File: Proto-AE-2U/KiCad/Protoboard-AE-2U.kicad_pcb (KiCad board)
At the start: 2 copper layers, 1 part

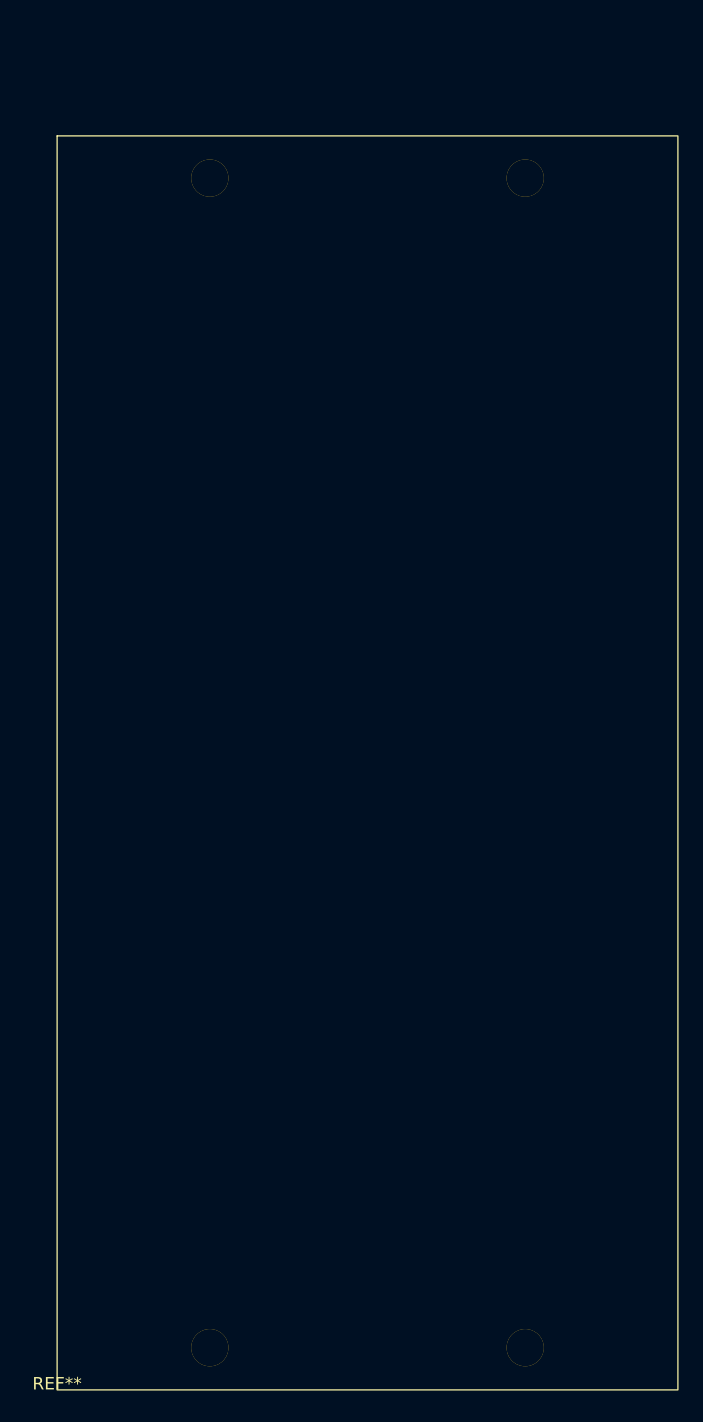
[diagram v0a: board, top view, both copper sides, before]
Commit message: copied 1U protoboard 2U and will adapt
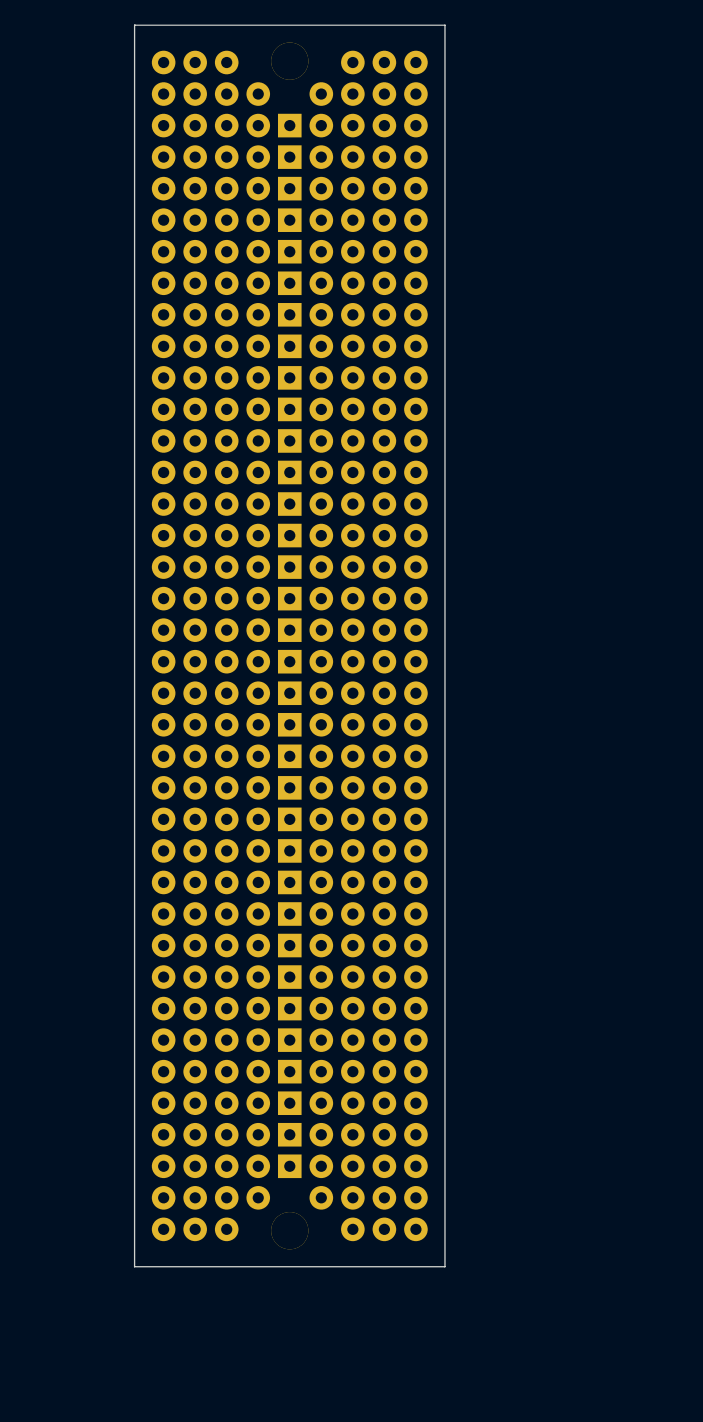
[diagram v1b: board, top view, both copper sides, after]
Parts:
- removed the REF** at (76.5, 144.0)
- added REF**: Pad, clectric-diy:Pad, F.Cu at (100.3, 47.2)
- added REF**: Pad, clectric-diy:Pad, F.Cu at (102.9, 42.2)
- added REF**: Pad, clectric-diy:Pad, F.Cu at (95.2, 95.5)
- added REF**: Pad, clectric-diy:Pad, F.Cu at (85.1, 42.2)
- added REF**: Pad, clectric-diy:Pad, F.Cu at (105.4, 54.9)
- added REF**: Pad, clectric-diy:Pad, F.Cu at (95.2, 85.3)
- added REF**: Pad, clectric-diy:Pad, F.Cu at (102.9, 44.7)
- added REF**: Pad, clectric-diy:Pad, F.Cu at (100.3, 108.2)
- added REF**: Pad, clectric-diy:Pad, F.Cu at (87.6, 100.6)
- added REF**: Pad, clectric-diy:Pad, F.Cu at (95.2, 67.6)
- added REF**: Pad, clectric-diy:Pad, F.Cu at (102.9, 80.3)
- added REF**: Pad, clectric-diy:Pad, F.Cu at (102.9, 57.4)
- added REF**: Pad, clectric-diy:Pad, F.Cu at (100.3, 103.1)
- added REF**: Pad, clectric-diy:Pad, F.Cu at (87.6, 115.8)
- added REF**: Pad, clectric-diy:Pad, F.Cu at (105.4, 110.8)
- added REF**: Pad, clectric-diy:Pad, F.Cu at (92.7, 75.2)
- added REF**: Pad, clectric-diy:Pad, F.Cu at (87.6, 49.8)
- added REF**: Pad, clectric-diy:Pad, F.Cu at (90.2, 57.4)
- added REF**: Pad, clectric-diy:Pad, F.Cu at (95.2, 103.1)
- added REF**: Pad, clectric-diy:Pad, F.Cu at (87.6, 44.7)
- added REF**: Pad, clectric-diy:Pad, F.Cu at (85.1, 82.8)
- added REF**: Pad, clectric-diy:Pad, F.Cu at (97.8, 42.2)
- added REF**: Pad, clectric-diy:Pad, F.Cu at (95.2, 123.5)
- added REF**: Pad, clectric-diy:Pad, F.Cu at (85.1, 47.2)
- added REF**: Pad, clectric-diy:Pad, F.Cu at (100.3, 93.0)
- added REF**: Pad, clectric-diy:Pad, F.Cu at (92.7, 110.8)
- added REF**: Pad, clectric-diy:Pad, F.Cu at (97.8, 85.3)
- added REF**: Pad, clectric-diy:Pad, F.Cu at (102.9, 113.3)
- added REF**: Pad, clectric-diy:Pad, F.Cu at (85.1, 37.1)
- added REF**: Pad, clectric-diy:Pad, F.Cu at (105.4, 123.5)
- added REF**: Pad, clectric-diy:Pad, F.Cu at (95.2, 113.3)
- added REF**: Pad, clectric-diy:Pad, F.Cu at (85.1, 80.3)
- added REF**: Pad, clectric-diy:Pad, F.Cu at (97.8, 115.8)
- added REF**: Pad, clectric-diy:Pad, F.Cu at (95.2, 47.2)
- added REF**: Pad, clectric-diy:Pad, F.Cu at (85.1, 98.0)
- added REF**: Pad, clectric-diy:Pad, F.Cu at (92.7, 105.7)
- added REF**: Pad, clectric-diy:Pad, F.Cu at (85.1, 49.8)
- added REF**: Pad, clectric-diy:Pad, F.Cu at (102.9, 75.2)
- added REF**: Pad, clectric-diy:Pad, F.Cu at (87.6, 39.6)
- added REF**: Pad, clectric-diy:Pad, F.Cu at (92.7, 100.6)
- added REF**: Pad, clectric-diy:Pad, F.Cu at (100.3, 87.9)
- added REF**: Pad, clectric-diy:Pad, F.Cu at (105.4, 47.2)
- added REF**: Pad, clectric-diy:Pad, F.Cu at (90.2, 85.3)
- added REF**: Pad, clectric-diy:Pad, F.Cu at (90.2, 105.7)
- added REF**: Pad, clectric-diy:Pad, F.Cu at (100.3, 67.6)
- added REF**: Pad, clectric-diy:Pad, F.Cu at (87.6, 85.3)
- added REF**: Pad, clectric-diy:Pad, F.Cu at (97.8, 52.3)
- added REF**: Pad, clectric-diy:Pad, F.Cu at (100.3, 90.4)
- added REF**: Pad, clectric-diy:Pad, F.Cu at (95.2, 118.4)
- added REF**: Pad, clectric-diy:Pad, F.Cu at (90.2, 113.3)
- added REF**: Pad, clectric-diy:Pad, F.Cu at (87.6, 98.0)
- added REF**: Pad, clectric-diy:Pad, F.Cu at (95.2, 49.8)
- added REF**: Pad, clectric-diy:Pad, F.Cu at (105.4, 113.3)
- added REF**: Pad, clectric-diy:Pad, F.Cu at (100.3, 72.7)
- added REF**: Pad, clectric-diy:Pad, F.Cu at (97.8, 80.3)
- added REF**: Pad, clectric-diy:Pad, F.Cu at (90.2, 118.4)
- added REF**: Pad, clectric-diy:Pad, F.Cu at (105.4, 95.5)
- added REF**: Pad, clectric-diy:Pad, F.Cu at (87.6, 70.1)
- added REF**: Pad, clectric-diy:Pad, F.Cu at (87.6, 128.5)
- added REF**: Pad, clectric-diy:Pad, F.Cu at (100.3, 98.0)
- added REF**: Pad, clectric-diy:Pad, F.Cu at (87.6, 60.0)
- added REF**: Pad, clectric-diy:Pad, F.Cu at (97.8, 57.4)
- added REF**: Pad, clectric-diy:Pad, F.Cu at (97.8, 100.6)
- added REF**: Pad, clectric-diy:Pad, F.Cu at (105.4, 77.7)
- added REF**: Pad, clectric-diy:Pad, F.Cu at (90.2, 90.4)
- added REF**: Pad, clectric-diy:Pad, F.Cu at (87.6, 131.1)
- added REF**: Pad, clectric-diy:Pad, F.Cu at (105.4, 98.0)
- added REF**: Pad, clectric-diy:Pad, F.Cu at (85.1, 128.5)
- added REF**: Pad, clectric-diy:Pad, F.Cu at (90.2, 47.2)
- added REF**: Pad, clectric-diy:Pad, F.Cu at (95.2, 52.3)
- added REF**: Pad, clectric-diy:Pad, F.Cu at (87.6, 37.1)
- added REF**: Pad, clectric-diy:Pad, F.Cu at (92.7, 95.5)
- added REF**: Pad, clectric-diy:Pad, F.Cu at (95.2, 136.2)
- added REF**: Pad, clectric-diy:Pad, F.Cu at (97.8, 39.6)
- added REF**: Pad, clectric-diy:Pad, F.Cu at (92.7, 85.3)
- added REF**: Pad, clectric-diy:Pad, F.Cu at (97.8, 67.6)
- added REF**: Pad, clectric-diy:Pad, F.Cu at (92.7, 93.0)
- added REF**: Pad, clectric-diy:Pad, F.Cu at (95.2, 60.0)
- added REF**: Pad, clectric-diy:Pad, F.Cu at (87.6, 123.5)
- added REF**: Pad, clectric-diy:Pad, F.Cu at (85.1, 87.9)
- added REF**: Pad, clectric-diy:Pad, F.Cu at (105.4, 128.5)
- added REF**: Pad, clectric-diy:Pad, F.Cu at (100.3, 110.8)
- added REF**: Pad, clectric-diy:Pad, F.Cu at (100.3, 42.2)
- added REF**: Pad, clectric-diy:Pad, F.Cu at (102.9, 70.1)
- added REF**: Pad, clectric-diy:Pad, F.Cu at (105.4, 57.4)
- added REF**: Pad, clectric-diy:Pad, F.Cu at (90.2, 120.9)
- added REF**: Pad, clectric-diy:Pad, F.Cu at (102.9, 52.3)
- added REF**: Pad, clectric-diy:Pad, F.Cu at (95.2, 62.5)
- added REF**: Pad, clectric-diy:Pad, F.Cu at (85.1, 85.3)
- added REF**: Pad, clectric-diy:Pad, F.Cu at (87.6, 126.0)
- added REF**: Pad, clectric-diy:Pad, F.Cu at (90.2, 100.6)
- added REF**: Pad, clectric-diy:Pad, F.Cu at (90.2, 93.0)
- added REF**: Pad, clectric-diy:Pad, F.Cu at (95.2, 108.2)
- added REF**: Pad, clectric-diy:Pad, F.Cu at (100.3, 54.9)
- added REF**: Pad, clectric-diy:Pad, F.Cu at (90.2, 115.8)
- added REF**: Pad, clectric-diy:Pad, F.Cu at (102.9, 90.4)
- added REF**: Pad, clectric-diy:Pad, F.Cu at (95.2, 105.7)
- added REF**: Pad, clectric-diy:Pad, F.Cu at (100.3, 60.0)
- added REF**: Pad, clectric-diy:Pad, F.Cu at (97.8, 93.0)
- added REF**: Pad, clectric-diy:Pad, F.Cu at (90.2, 110.8)
- added REF**: Pad, clectric-diy:Pad, F.Cu at (100.3, 39.6)
- added REF**: Pad, clectric-diy:Pad, F.Cu at (90.2, 62.5)
- added REF**: Pad, clectric-diy:Pad, F.Cu at (105.4, 85.3)
- added REF**: Pad, clectric-diy:Pad, F.Cu at (102.9, 72.7)
- added REF**: Pad, clectric-diy:Pad, F.Cu at (87.6, 118.4)
- added REF**: Pad, clectric-diy:Pad, F.Cu at (92.7, 118.4)
- added REF**: Pad, clectric-diy:Pad, F.Cu at (105.4, 126.0)
- added REF**: Pad, clectric-diy:Pad, F.Cu at (100.3, 49.8)
- added REF**: Pad, clectric-diy:Pad, F.Cu at (92.7, 72.7)
- added REF**: Pad, clectric-diy:Pad, F.Cu at (90.2, 42.2)
- added REF**: Pad, clectric-diy:Pad, F.Cu at (105.4, 103.1)
- added REF**: Pad, clectric-diy:Pad, F.Cu at (90.2, 60.0)
- added REF**: Pad, clectric-diy:Pad, F.Cu at (100.3, 80.3)
- added REF**: Pad, clectric-diy:Pad, F.Cu at (97.8, 105.7)
- added REF**: Pad, clectric-diy:Pad, F.Cu at (100.3, 62.5)
- added REF**: Pad, clectric-diy:Pad, F.Cu at (90.2, 72.7)
- added REF**: Pad, clectric-diy:Pad, F.Cu at (105.4, 118.4)
- added REF**: Pad, clectric-diy:Pad, F.Cu at (85.1, 39.6)
- added REF**: Pad, clectric-diy:Pad, F.Cu at (95.2, 77.7)
- added REF**: Pad, clectric-diy:Pad, F.Cu at (90.2, 49.8)
- added REF**: Pad, clectric-diy:Pad, F.Cu at (105.4, 115.8)
- added REF**: Pad, clectric-diy:Pad, F.Cu at (95.2, 98.0)
- added REF**: Pad, clectric-diy:Pad, F.Cu at (97.8, 113.3)
- added REF**: Pad, clectric-diy:Pad, F.Cu at (97.8, 110.8)
- added REF**: Pad, clectric-diy:Pad, F.Cu at (97.8, 47.2)
- added REF**: Pad, clectric-diy:Pad, F.Cu at (85.1, 105.7)
- added REF**: Pad, clectric-diy:Pad, F.Cu at (92.7, 44.7)
- added REF**: Pad, clectric-diy:Pad, F.Cu at (85.1, 57.4)
- added REF**: Pad, clectric-diy:Pad, F.Cu at (92.7, 52.3)
- added REF**: Pad, clectric-diy:Pad, F.Cu at (100.3, 126.0)
- added REF**: Pad, clectric-diy:Pad, F.Cu at (102.9, 62.5)
- added REF**: Pad, clectric-diy:Pad, F.Cu at (105.4, 42.2)
- added REF**: Pad, clectric-diy:Pad, F.Cu at (92.7, 42.2)
- added REF**: Pad, clectric-diy:Pad, F.Cu at (105.4, 52.3)
- added REF**: Pad, clectric-diy:Pad, F.Cu at (85.1, 118.4)
- added REF**: Pad, clectric-diy:Pad, F.Cu at (92.7, 47.2)
- added REF**: Pad, clectric-diy:Pad, F.Cu at (90.2, 52.3)
- added REF**: Pad, clectric-diy:Pad, F.Cu at (92.7, 70.1)
- added REF**: Pad, clectric-diy:Pad, F.Cu at (95.2, 80.3)
- added REF**: Pad, clectric-diy:Pad, F.Cu at (97.8, 123.5)
- added REF**: Pad, clectric-diy:Pad, F.Cu at (102.9, 115.8)
- added REF**: Pad, clectric-diy:Pad, F.Cu at (95.2, 54.9)
- added REF**: Pad, clectric-diy:Pad, F.Cu at (102.9, 131.1)
- added REF**: Pad, clectric-diy:Pad, F.Cu at (105.4, 75.2)
- added REF**: Pad, clectric-diy:Pad, F.Cu at (85.1, 77.7)
- added REF**: Pad, clectric-diy:Pad, F.Cu at (90.2, 108.2)
- added REF**: Pad, clectric-diy:Pad, F.Cu at (100.3, 113.3)
- added REF**: Pad, clectric-diy:Pad, F.Cu at (92.7, 49.8)
- added REF**: Pad, clectric-diy:Pad, F.Cu at (95.2, 90.4)
- added REF**: Pad, clectric-diy:Pad, F.Cu at (100.3, 115.8)
- added REF**: Pad, clectric-diy:Pad, F.Cu at (87.6, 52.3)
- added REF**: Pad, clectric-diy:Pad, F.Cu at (90.2, 80.3)
- added REF**: Pad, clectric-diy:Pad, F.Cu at (87.6, 108.2)
- added REF**: Pad, clectric-diy:Pad, F.Cu at (97.8, 82.8)
- added REF**: Pad, clectric-diy:Pad, F.Cu at (105.4, 72.7)
- added REF**: Pad, clectric-diy:Pad, F.Cu at (92.7, 126.0)
- added REF**: Pad, clectric-diy:Pad, F.Cu at (87.6, 113.3)
- added REF**: Pad, clectric-diy:Pad, F.Cu at (85.1, 90.4)
- added REF**: Pad, clectric-diy:Pad, F.Cu at (102.9, 95.5)
- added REF**: Pad, clectric-diy:Pad, F.Cu at (102.9, 60.0)
- added REF**: Pad, clectric-diy:Pad, F.Cu at (87.6, 120.9)
- added REF**: Pad, clectric-diy:Pad, F.Cu at (95.2, 110.8)
- added REF**: Pad, clectric-diy:Pad, F.Cu at (97.8, 103.1)
- added REF**: Pad, clectric-diy:Pad, F.Cu at (102.9, 123.5)
- added REF**: Pad, clectric-diy:Pad, F.Cu at (85.1, 115.8)
- added REF**: Pad, clectric-diy:Pad, F.Cu at (95.2, 65.0)
- added REF**: Pad, clectric-diy:Pad, F.Cu at (85.1, 95.5)
- added REF**: Pad, clectric-diy:Pad, F.Cu at (100.3, 100.6)
- added REF**: Pad, clectric-diy:Pad, F.Cu at (102.9, 87.9)
- added REF**: Pad, clectric-diy:Pad, F.Cu at (105.4, 60.0)
- added REF**: Pad, clectric-diy:Pad, F.Cu at (92.7, 120.9)
- added REF**: Pad, clectric-diy:Pad, F.Cu at (95.2, 126.0)
- added REF**: Pad, clectric-diy:Pad, F.Cu at (102.9, 120.9)
- added REF**: Pad, clectric-diy:Pad, F.Cu at (102.9, 39.6)
- added REF**: Pad, clectric-diy:Pad, F.Cu at (105.4, 62.5)
- added REF**: Pad, clectric-diy:Pad, F.Cu at (105.4, 120.9)
- added REF**: Pad, clectric-diy:Pad, F.Cu at (92.7, 82.8)
- added REF**: Pad, clectric-diy:Pad, F.Cu at (85.1, 110.8)
- added REF**: Pad, clectric-diy:Pad, F.Cu at (92.7, 65.0)
- added REF**: Pad, clectric-diy:Pad, F.Cu at (100.3, 85.3)
- added REF**: Pad, clectric-diy:Pad, F.Cu at (102.9, 47.2)
- added REF**: Pad, clectric-diy:Pad, F.Cu at (85.1, 52.3)
- added REF**: Pad, clectric-diy:Pad, F.Cu at (102.9, 103.1)
- added REF**: Pad, clectric-diy:Pad, F.Cu at (92.7, 57.4)
- added REF**: Pad, clectric-diy:Pad, F.Cu at (92.7, 123.5)
- added REF**: Pad, clectric-diy:Pad, F.Cu at (92.7, 113.3)
- added REF**: Pad, clectric-diy:Pad, F.Cu at (102.9, 93.0)
- added REF**: Pad, clectric-diy:Pad, F.Cu at (87.6, 80.3)
- added REF**: Pad, clectric-diy:Pad, F.Cu at (102.9, 49.8)
- added REF**: Pad, clectric-diy:Pad, F.Cu at (95.2, 120.9)
- added REF**: Pad, clectric-diy:Pad, F.Cu at (90.2, 39.6)
- added REF**: Pad, clectric-diy:Pad, F.Cu at (102.9, 126.0)
- added REF**: Pad, clectric-diy:Pad, F.Cu at (97.8, 75.2)
- added REF**: Pad, clectric-diy:Pad, F.Cu at (100.3, 131.1)
- added REF**: Pad, clectric-diy:Pad, F.Cu at (87.6, 67.6)
- added REF**: Pad, clectric-diy:Pad, F.Cu at (90.2, 65.0)
- added REF**: Pad, clectric-diy:Pad, F.Cu at (105.4, 44.7)
- added REF**: Pad, clectric-diy:Pad, F.Cu at (105.4, 100.6)
- added REF**: Pad, clectric-diy:Pad, F.Cu at (87.6, 75.2)
- added REF**: Pad, clectric-diy:Pad, F.Cu at (87.6, 72.7)
- added REF**: Pad, clectric-diy:Pad, F.Cu at (92.7, 87.9)
- added REF**: Pad, clectric-diy:Pad, F.Cu at (85.1, 44.7)
- added REF**: Pad, clectric-diy:Pad, F.Cu at (105.4, 105.7)
- added REF**: Pad, clectric-diy:Pad, F.Cu at (102.9, 118.4)
- added REF**: Pad, clectric-diy:Pad, F.Cu at (105.4, 70.1)
- added REF**: Pad, clectric-diy:Pad, F.Cu at (100.3, 123.5)
- added REF**: Pad, clectric-diy:Pad, F.Cu at (105.4, 67.6)
- added REF**: Pad, clectric-diy:Pad, F.Cu at (105.4, 90.4)
- added REF**: Pad, clectric-diy:Pad, F.Cu at (85.1, 123.5)
- added REF**: Pad, clectric-diy:Pad, F.Cu at (85.1, 108.2)
- added REF**: Pad, clectric-diy:Pad, F.Cu at (102.9, 100.6)
- added REF**: Pad, clectric-diy:Pad, F.Cu at (90.2, 126.0)
- added REF**: Pad, clectric-diy:Pad, F.Cu at (102.9, 98.0)
- added REF**: Pad, clectric-diy:Pad, F.Cu at (87.6, 87.9)
- added REF**: Pad, clectric-diy:Pad, F.Cu at (97.8, 72.7)
- added REF**: Pad, clectric-diy:Pad, F.Cu at (102.9, 128.5)
- added REF**: Pad, clectric-diy:Pad, F.Cu at (85.1, 60.0)
- added REF**: Pad, clectric-diy:Pad, F.Cu at (87.6, 47.2)
- added REF**: Pad, clectric-diy:Pad, F.Cu at (87.6, 62.5)
- added REF**: Pad, clectric-diy:Pad, F.Cu at (97.8, 118.4)
- added REF**: Pad, clectric-diy:Pad, F.Cu at (95.2, 70.1)
- added REF**: Pad, clectric-diy:Pad, F.Cu at (87.6, 103.1)
- added REF**: Pad, clectric-diy:Pad, F.Cu at (90.2, 87.9)
- added REF**: Pad, clectric-diy:Pad, F.Cu at (102.9, 105.7)
- added REF**: Pad, clectric-diy:Pad, F.Cu at (100.3, 128.5)
- added REF**: Pad, clectric-diy:Pad, F.Cu at (92.7, 39.6)
- added REF**: Pad, clectric-diy:Pad, F.Cu at (87.6, 105.7)
- added REF**: Pad, clectric-diy:Pad, F.Cu at (97.8, 98.0)
- added REF**: Pad, clectric-diy:Pad, F.Cu at (105.4, 93.0)
- added REF**: Pad, clectric-diy:Pad, F.Cu at (102.9, 67.6)
- added REF**: Pad, clectric-diy:Pad, F.Cu at (102.9, 82.8)
- added REF**: Pad, clectric-diy:Pad, F.Cu at (97.8, 108.2)
- added REF**: Pad, clectric-diy:Pad, F.Cu at (90.2, 70.1)
- added REF**: Pad, clectric-diy:Pad, F.Cu at (97.8, 90.4)
- added REF**: Pad, clectric-diy:Pad, F.Cu at (85.1, 120.9)
- added REF**: Pad, clectric-diy:Pad, F.Cu at (87.6, 42.2)
- added REF**: Pad, clectric-diy:Pad, F.Cu at (92.7, 103.1)
- added REF**: Pad, clectric-diy:Pad, F.Cu at (95.2, 75.2)
- added REF**: Pad, clectric-diy:Pad, F.Cu at (87.6, 110.8)
- added REF**: Pad, clectric-diy:Pad, F.Cu at (90.2, 103.1)
- added REF**: Pad, clectric-diy:Pad, F.Cu at (105.4, 49.8)
- added REF**: Pad, clectric-diy:Pad, F.Cu at (100.3, 37.1)
- added REF**: Pad, clectric-diy:Pad, F.Cu at (95.2, 93.0)
- added REF**: Pad, clectric-diy:Pad, F.Cu at (97.8, 95.5)
- added REF**: Pad, clectric-diy:Pad, F.Cu at (90.2, 67.6)
- added REF**: Pad, clectric-diy:Pad, F.Cu at (97.8, 49.8)
- added REF**: Pad, clectric-diy:Pad, F.Cu at (102.9, 77.7)
- added REF**: Pad, clectric-diy:Pad, F.Cu at (95.2, 42.2)
- added REF**: Pad, clectric-diy:Pad, F.Cu at (92.7, 60.0)
- added REF**: Pad, clectric-diy:Pad, F.Cu at (97.8, 65.0)
- added REF**: Pad, clectric-diy:Pad, F.Cu at (100.3, 82.8)
- added REF**: Pad, clectric-diy:Pad, F.Cu at (105.4, 87.9)
- added REF**: Pad, clectric-diy:Pad, F.Cu at (100.3, 65.0)
- added REF**: Pad, clectric-diy:Pad, F.Cu at (105.4, 131.1)
- added REF**: Pad, clectric-diy:Pad, F.Cu at (85.1, 67.6)
- added REF**: Pad, clectric-diy:Pad, F.Cu at (95.2, 44.7)
- added REF**: Pad, clectric-diy:Pad, F.Cu at (105.4, 37.1)
- added REF**: Pad, clectric-diy:Pad, F.Cu at (95.2, 37.0)
- added REF**: Pad, clectric-diy:Pad, F.Cu at (102.9, 65.0)
- added REF**: Pad, clectric-diy:Pad, F.Cu at (92.7, 77.7)
- added REF**: Pad, clectric-diy:Pad, F.Cu at (100.3, 44.7)
- added REF**: Pad, clectric-diy:Pad, F.Cu at (90.2, 131.1)
- added REF**: Pad, clectric-diy:Pad, F.Cu at (100.3, 57.4)
- added REF**: Pad, clectric-diy:Pad, F.Cu at (92.7, 128.5)
- added REF**: Pad, clectric-diy:Pad, F.Cu at (100.3, 105.7)
- added REF**: Pad, clectric-diy:Pad, F.Cu at (100.3, 77.7)
- added REF**: Pad, clectric-diy:Pad, F.Cu at (87.6, 57.4)
- added REF**: Pad, clectric-diy:Pad, F.Cu at (87.6, 65.0)
- added REF**: Pad, clectric-diy:Pad, F.Cu at (100.3, 95.5)
- added REF**: Pad, clectric-diy:Pad, F.Cu at (97.8, 120.9)
- added REF**: Pad, clectric-diy:Pad, F.Cu at (90.2, 54.9)
- added REF**: Pad, clectric-diy:Pad, F.Cu at (90.2, 128.5)
- added REF**: Pad, clectric-diy:Pad, F.Cu at (95.2, 72.7)
- added REF**: Pad, clectric-diy:Pad, F.Cu at (87.6, 93.0)
- added REF**: Pad, clectric-diy:Pad, F.Cu at (87.6, 90.4)
- added REF**: Pad, clectric-diy:Pad, F.Cu at (90.2, 77.7)
- added REF**: Pad, clectric-diy:Pad, F.Cu at (97.8, 62.5)
- added REF**: Pad, clectric-diy:Pad, F.Cu at (95.2, 57.4)
- added REF**: Pad, clectric-diy:Pad, F.Cu at (102.9, 110.8)
- added REF**: Pad, clectric-diy:Pad, F.Cu at (92.7, 115.8)
- added REF**: Pad, clectric-diy:Pad, F.Cu at (85.1, 54.9)
- added REF**: Pad, clectric-diy:Pad, F.Cu at (92.7, 67.6)
- added REF**: Pad, clectric-diy:Pad, F.Cu at (95.2, 100.6)
- added REF**: Pad, clectric-diy:Pad, F.Cu at (92.7, 90.4)
- added REF**: Pad, clectric-diy:Pad, F.Cu at (95.2, 87.9)
- added REF**: Pad, clectric-diy:Pad, F.Cu at (92.7, 98.0)
- added REF**: Pad, clectric-diy:Pad, F.Cu at (100.3, 75.2)
- added REF**: Pad, clectric-diy:Pad, F.Cu at (92.7, 108.2)
- added REF**: Pad, clectric-diy:Pad, F.Cu at (97.8, 128.5)
- added REF**: Pad, clectric-diy:Pad, F.Cu at (90.2, 123.5)
- added REF**: Pad, clectric-diy:Pad, F.Cu at (95.2, 115.8)
- added REF**: Pad, clectric-diy:Pad, F.Cu at (85.1, 72.7)
- added REF**: Pad, clectric-diy:Pad, F.Cu at (90.2, 98.0)
- added REF**: Pad, clectric-diy:Pad, F.Cu at (97.8, 126.0)
- added REF**: Pad, clectric-diy:Pad, F.Cu at (85.1, 103.1)
- added REF**: Pad, clectric-diy:Pad, F.Cu at (92.7, 54.9)
- added REF**: Pad, clectric-diy:Pad, F.Cu at (97.8, 44.7)
- added REF**: Pad, clectric-diy:Pad, F.Cu at (100.3, 120.9)
- added REF**: Pad, clectric-diy:Pad, F.Cu at (90.2, 82.8)
- added REF**: Pad, clectric-diy:Pad, F.Cu at (90.2, 44.7)
- added REF**: Pad, clectric-diy:Pad, F.Cu at (102.9, 108.2)
- added REF**: Pad, clectric-diy:Pad, F.Cu at (85.1, 113.3)
- added REF**: Pad, clectric-diy:Pad, F.Cu at (85.1, 62.5)
- added REF**: Pad, clectric-diy:Pad, F.Cu at (97.8, 77.7)
- added REF**: Pad, clectric-diy:Pad, F.Cu at (97.8, 60.0)
- added REF**: Pad, clectric-diy:Pad, F.Cu at (90.2, 37.1)
- added REF**: Pad, clectric-diy:Pad, F.Cu at (85.1, 126.0)
- added REF**: Pad, clectric-diy:Pad, F.Cu at (100.3, 118.4)
- added REF**: Pad, clectric-diy:Pad, F.Cu at (105.4, 39.6)
- added REF**: Pad, clectric-diy:Pad, F.Cu at (95.2, 82.8)
- added REF**: Pad, clectric-diy:Pad, F.Cu at (87.6, 54.9)
- added REF**: Pad, clectric-diy:Pad, F.Cu at (85.1, 100.6)
- added REF**: Pad, clectric-diy:Pad, F.Cu at (105.4, 65.0)
- added REF**: Pad, clectric-diy:Pad, F.Cu at (87.6, 82.8)
- added REF**: Pad, clectric-diy:Pad, F.Cu at (105.4, 80.3)
- added REF**: Pad, clectric-diy:Pad, F.Cu at (85.1, 131.1)
- added REF**: Pad, clectric-diy:Pad, F.Cu at (87.6, 77.7)
- added REF**: Pad, clectric-diy:Pad, F.Cu at (92.7, 80.3)
- added REF**: Pad, clectric-diy:Pad, F.Cu at (85.1, 75.2)
- added REF**: Pad, clectric-diy:Pad, F.Cu at (85.1, 65.0)
- added REF**: Pad, clectric-diy:Pad, F.Cu at (87.6, 95.5)
- added REF**: Pad, clectric-diy:Pad, F.Cu at (97.8, 87.9)
- added REF**: Pad, clectric-diy:Pad, F.Cu at (100.3, 52.3)
- added REF**: Pad, clectric-diy:Pad, F.Cu at (97.8, 54.9)
- added REF**: Pad, clectric-diy:Pad, F.Cu at (105.4, 108.2)
- added REF**: Pad, clectric-diy:Pad, F.Cu at (85.1, 70.1)
- added REF**: Pad, clectric-diy:Pad, F.Cu at (97.8, 70.1)
- added REF**: Pad, clectric-diy:Pad, F.Cu at (102.9, 85.3)
- added REF**: Pad, clectric-diy:Pad, F.Cu at (102.9, 37.1)
- added REF**: Pad, clectric-diy:Pad, F.Cu at (85.1, 93.0)
- added REF**: Pad, clectric-diy:Pad, F.Cu at (90.2, 95.5)
- added REF**: Pad, clectric-diy:Pad, F.Cu at (90.2, 75.2)
- added REF**: Pad, clectric-diy:Pad, F.Cu at (105.4, 82.8)
- added REF**: Pad, clectric-diy:Pad, F.Cu at (100.3, 70.1)
- added REF**: Pad, clectric-diy:Pad, F.Cu at (92.7, 62.5)
- added REF**: Pad, clectric-diy:Pad, F.Cu at (102.9, 54.9)
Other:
- board outline added: 25 x 100 mm
